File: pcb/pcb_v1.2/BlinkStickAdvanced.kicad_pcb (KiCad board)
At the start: 2 copper layers, 37.1 x 59.3 mm, 34 parts, among them J1 POWER, J2 USB_B_Micro, J3 ADD_HEADER_B, J4 ADD_HEADER_G, J5 ADD_HEADER_R, J6 RGB_HEADER, J7 RGB_HEADER, Q1 IRLR8726, Q2 IRLR8726, Q3 IRLR8726, U1 ATmega8-16A, Y1 Crystal_GND2_Small

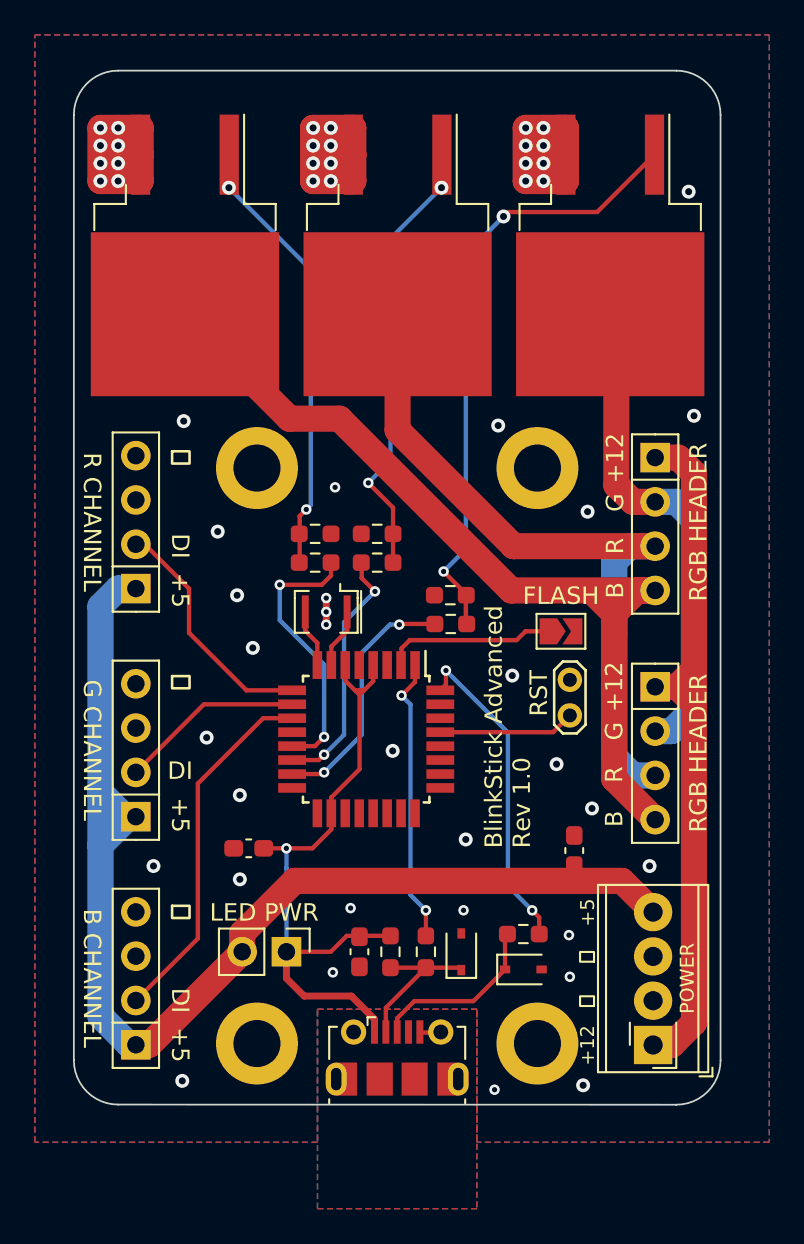
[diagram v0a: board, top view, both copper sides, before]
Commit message: Move old PCB files to a different folder.
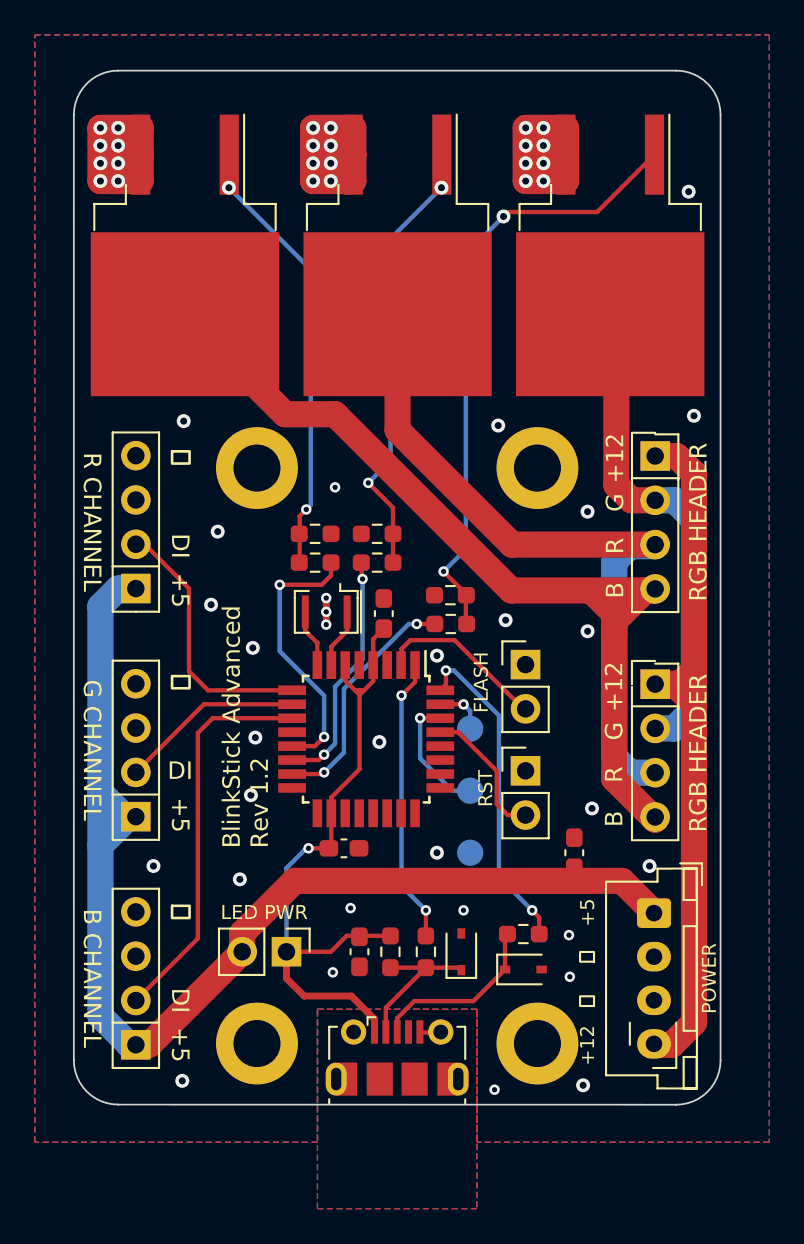
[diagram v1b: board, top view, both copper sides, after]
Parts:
- removed JP1: RST, TestPoint:TestPoint_2Pads_Pitch2.54mm_Drill0.8mm
- removed JP2: FLASH, Jumper:SolderJumper-2_P1.3mm_Open_TrianglePad1.0x1.5mm
- removed the REF** at (45.2, 43.3)
- added C4: 1uF, Capacitor_SMD:C_0603_1608Metric_Pad1.08x0.95mm_HandSolder, F.Cu at (56.4, 65.3)
- added J3: FLASH, Connector_PinHeader_2.54mm:PinHeader_1x02_P2.54mm_Vertical, F.Cu at (64.5, 68.2)
- added J9: POWER, Connector_JST:JST_XH_B4B-XH-A_1x04_P2.50mm_Vertical, F.Cu at (71.9, 82.5)
- added TP1: GND, TestPoint:TestPoint_Pad_D1.5mm, B.Cu at (61.3, 79.0)
- added TP2: RXD, TestPoint:TestPoint_Pad_D1.5mm, B.Cu at (61.3, 75.4)
- added TP3: TXD, TestPoint:TestPoint_Pad_D1.5mm, B.Cu at (61.3, 71.9)
- J1: value POWER -> RST; footprint TerminalBlock_Phoenix:TerminalBlock_Phoenix_MPT-0,5-4-2.54_1x04_P2.54mm_Horizontal -> Connector_PinHeader_2.54mm:PinHeader_1x02_P2.54mm_Vertical
- moved J1 17.3 mm to (64.5, 74.3), turned to 0 degrees
- moved C3 5.46 mm to (54.1, 78.7), turned to 180 degrees
- moved J7 0.15 mm to (71.9, 69.3)
- moved C1 0.13 mm to (67.3, 79.0)
- moved J8 0.09 mm to (71.9, 56.2)
- renumbered C3 to C1, C1 to C2, C2 to C3, D2 to D1, D1 to D2, J3 to J4, J4 to J5, J5 to J6, J6 to J7, J7 to J8
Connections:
- J1 pad 1: +12V -> GND
- J1 pad 2: GND -> Net-(U1-Pad29)
- U1 pad 30: unconnected-(U1-Pad30) -> /RXD
- U1 pad 31: unconnected-(U1-Pad31) -> /TXD
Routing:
- net /RXD: track 0.00 -> 7.11 mm, vias 0 -> 1
- net /TXD: track 0.00 -> 3.02 mm, vias 0 -> 1
- net /B_Channel: track 20.9 -> 22.6 mm
- net /R_Channel: track 13.9 -> 15.2 mm
- net +5V: track 38.0 -> 38.9 mm
- net /B_OUT: track 52.3 -> 51.5 mm
- net /G_PWM: track 14.5 -> 13.9 mm
- net Net-(U1-Pad2): track 9.53 -> 10.1 mm
- net /R_PWM: track 14.5 -> 13.9 mm
- net GND: vias 54 -> 55
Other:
- board text added: "BlinkStick Advanced Rev 1.2"
- board text removed: "BlinkStick Advanced Rev 1.0"
